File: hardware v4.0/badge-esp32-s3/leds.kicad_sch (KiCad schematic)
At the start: 32 parts

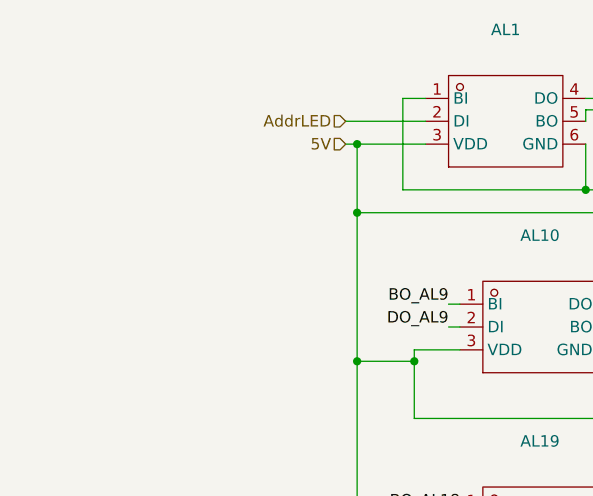
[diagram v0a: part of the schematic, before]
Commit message: added DRD, 3.3V switching reg, and VIN
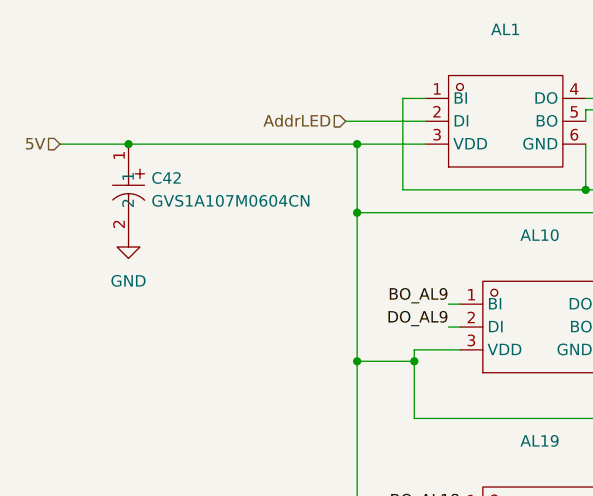
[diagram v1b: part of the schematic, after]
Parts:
- added C42: GVS1A107M0604CN, lcsc-lib:CAP-SMD_BD6.3-L6.6-W6.6-LS7.3-FD, symbol lcsc-lib:GVS1A107M0604CN
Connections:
- net 5V: now also C42.1
- net GND: now also C42.2
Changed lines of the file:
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@@
 	)
 	(junction
+		(at 31.75 62.23)
+		(diameter 0)
+		(color 0 0 0 0)
+	)
+	(junction
 		(at 220.98 90.17)
 		(diameter 0)
@@
 	(wire
 		(pts
-			(xy 55.88 62.23) (xy 57.15 62.23)
+			(xy 24.13 62.23) (xy 31.75 62.23)
 		)
 		(stroke
@@
 	(wire
 		(pts
+			(xy 31.75 62.23) (xy 57.15 62.23)
+		)
+		(stroke
+			(width 0)
+			(type default)
+		)
+	)
+	(wire
+		(pts
 			(xy 111.76 102.87) (xy 114.3 102.87)
 		)
@@
 	(hierarchical_label "5V"
 		(shape input)
-		(at 55.88 62.23 180)
+		(at 24.13 62.23 180)
 		(effects
 			(font
@@
 					(unit 1)
 				)
+			)
+		)
+	)
+	(symbol
+		(lib_id "power:GND")
+		(at 31.75 72.39 0)
+		(unit 1)
+		(exclude_from_sim no)
+		(in_bom yes)
+		(on_board yes)
+		(dnp no)
+		(fields_autoplaced yes)
+		(property "Reference" "#PWR092"
+			(at 31.75 78.74 0)
+			(effects
+				(font
+					(size 1.27 1.27)
+				)
+				(hide yes)
+			)
+		)
+		(property "Value" "GND"
+			(at 31.75 77.47 0)
+			(effects
+				(font
+					(size 1.27 1.27)
+				)
+			)
+		)
+		(property "Footprint" ""
+			(at 31.75 72.39 0)
+			(effects
+				(font
+					(size 1.27 1.27)
+				)
+				(hide yes)
+			)
+		)
+		(property "Datasheet" ""
+			(at 31.75 72.39 0)
+			(effects
+				(font
+					(size 1.27 1.27)
+				)
+				(hide yes)
+			)
+		)
+		(property "Description" "Power symbol creates a global label with name \"GND\" , ground"
+			(at 31.75 72.39 0)
+			(effects
+				(font
+					(size 1.27 1.27)
+				)
+				(hide yes)
+			)
+		)
+		(pin "1"
+		)
+		(instances
+			(project ""
+				(path "/e2af9a6c-dbe9-4de2-9ba6-ea213a7300ec/cf4b41f4-37f8-453c-b748-b2fe0c3fb5a0"
+					(reference "#PWR092")
+					(unit 1)
+				)
+			)
+		)
+	)
+	(symbol
+		(lib_id "lcsc-lib:GVS1A107M0604CN")
+		(at 31.75 67.31 270)
+		(unit 1)
+		(exclude_from_sim no)
+		(in_bom yes)
+		(on_board yes)
+		(dnp no)
+		(fields_autoplaced yes)
+		(property "Reference" "C42"
+			(at 34.29 66.0399 90)
+			(effects
+				(font
+					(size 1.27 1.27)
+				)
+				(justify left)
+			)
+		)
+		(property "Value" "GVS1A107M0604CN"
+			(at 34.29 68.5799 90)
+			(effects
+				(font
+					(size 1.27 1.27)
+				)
+				(justify left)
+			)
+		)
+		(property "Footprint" "lcsc-lib:CAP-SMD_BD6.3-L6.6-W6.6-LS7.3-FD"
+			(at 24.13 67.31 0)
+			(effects
+				(font
+					(size 1.27 1.27)
+				)
+				(hide yes)
+			)
+		)
+		(property "Datasheet" "https://www.lcsc.com/datasheet/C22383610.pdf"
+			(at 21.59 67.31 0)
+			(effects
+				(font
+					(size 1.27 1.27)
+				)
+				(hide yes)
+			)
+		)
+		(property "Description" ""
+			(at 31.75 67.31 0)
+			(effects
+				(font
+					(size 1.27 1.27)
+				)
+				(hide yes)
+			)
+		)
+		(property "Manufacturer" "ACMECON(鼎容)"
+			(at 19.05 67.31 0)
+			(effects
+				(font
+					(size 1.27 1.27)
+				)
+				(hide yes)
+			)
+		)
+		(property "MPN" "GVS1A107M0604CN"
+			(at 16.51 67.31 0)
+			(effects
+				(font
+					(size 1.27 1.27)
+				)
+				(hide yes)
+			)
+		)
+		(property "LCSC Part" "C22383610"
+			(at 13.97 67.31 0)
+			(effects
+				(font
+					(size 1.27 1.27)
+				)
+				(hide yes)
+			)
+		)
+		(pin "2"
+		)
+		(pin "1"
+		)
+		(instances
+			(project "badge-esp32-s3"
+				(path "/e2af9a6c-dbe9-4de2-9ba6-ea213a7300ec/cf4b41f4-37f8-453c-b748-b2fe0c3fb5a0"
+					(reference "C42")
+					(unit 1)
+				)
